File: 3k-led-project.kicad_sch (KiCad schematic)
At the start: 25 parts, among them SW1 SW_Push, U1 PRTR5V0U2X, U2 ATmega32U2-A, Y1 Crystal_GND24_Small

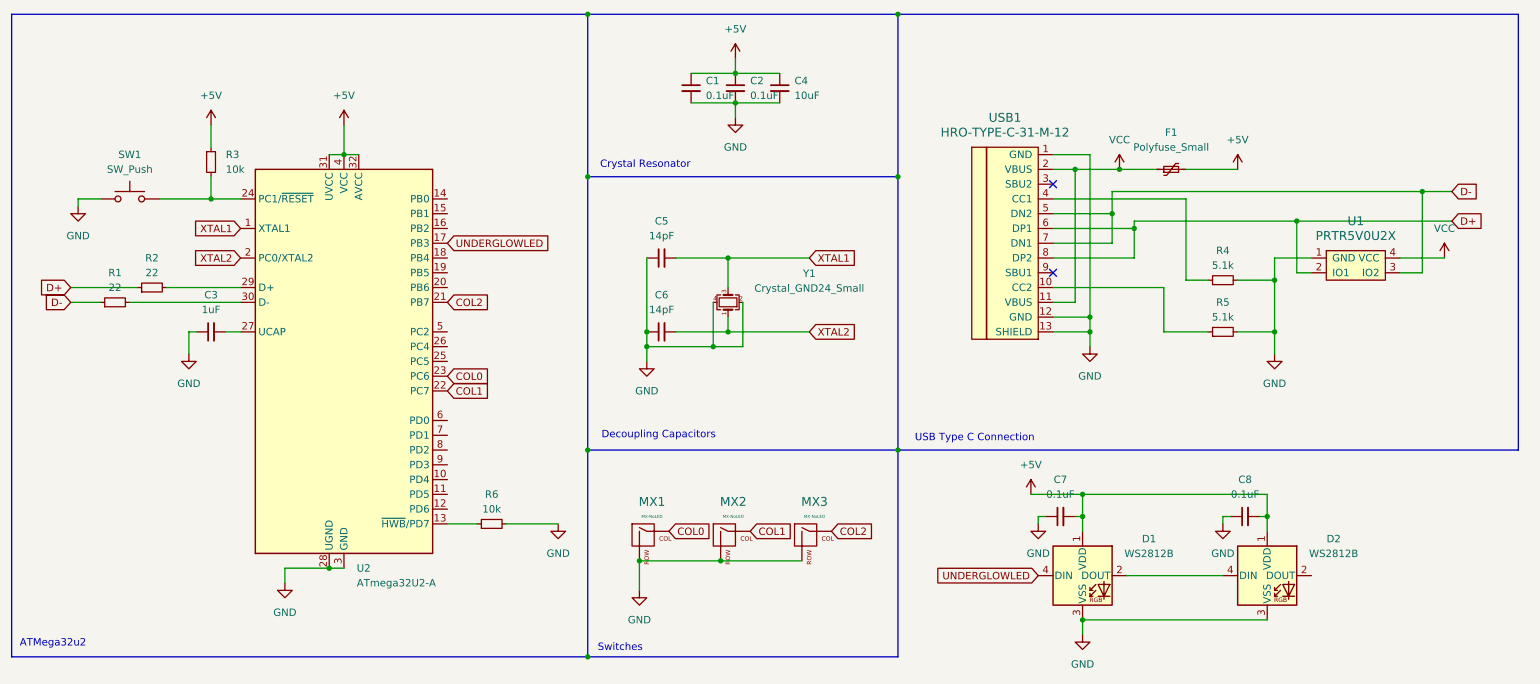
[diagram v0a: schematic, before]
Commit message: barfed the components into the pcb and updated schematic
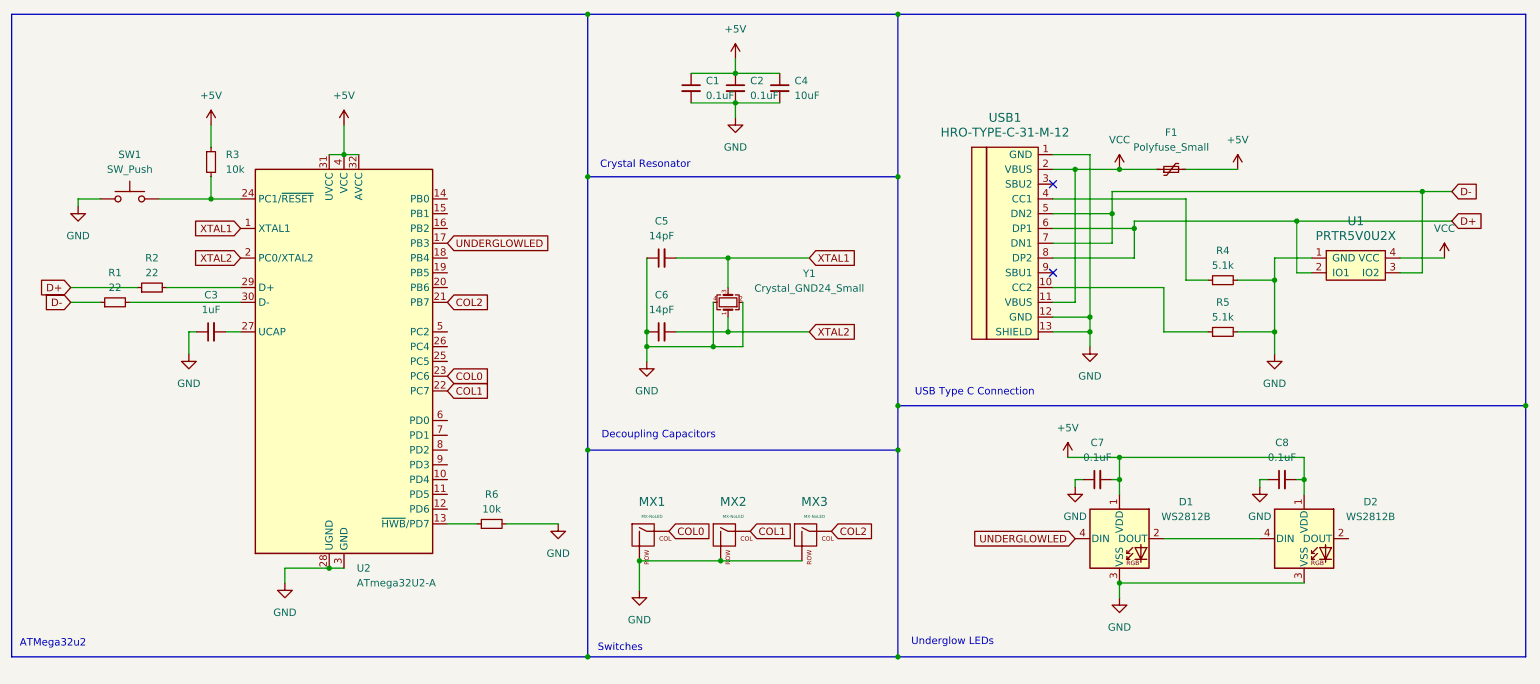
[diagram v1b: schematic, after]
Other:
- note added: "Underglow LEDs"
- moved on the sheet: C7, C8, D1, D2
